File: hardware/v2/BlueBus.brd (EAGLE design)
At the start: 95 x 65 mm, 140 parts, among them J1 3PIN_953442_1, J2 6PIN_953442_1, J3 6PIN_5_103166_1, J4 SJ2-35853A-SMT-TR, J5 SMB_CONN, J6 USB3080-30-01-A, J7 PCM12SMTR, J8 TC2030NL, Q1 NMOSFET-BSS138K, Q2 NMOSFET-BSS138K, Q3 PMOSFET-DMP32D4SSOT323, U1 MPQ4420, U10 PCM5122, U11 PAM8406, U2 TH3122.4, U3 FT231XS, U4 S-1212BC0-U5T1U, U5 XC6210, U6 CAT25M01, U7 PIC24FJ1024GA606, U8 BM83SM1, U9 DIT4096

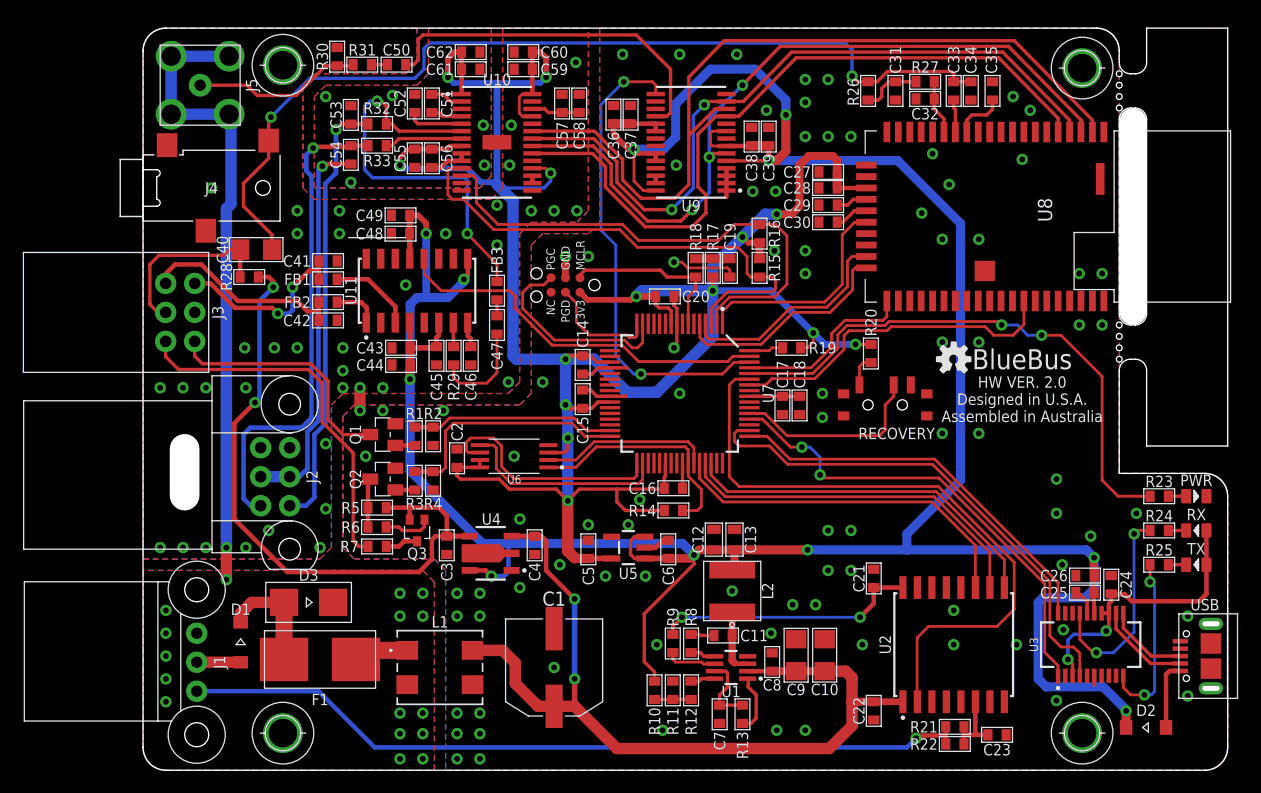
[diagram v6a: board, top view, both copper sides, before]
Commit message: [IMP] hardware: V2 silkscreen * Add fiducial markings * Fix issues with silkscreen
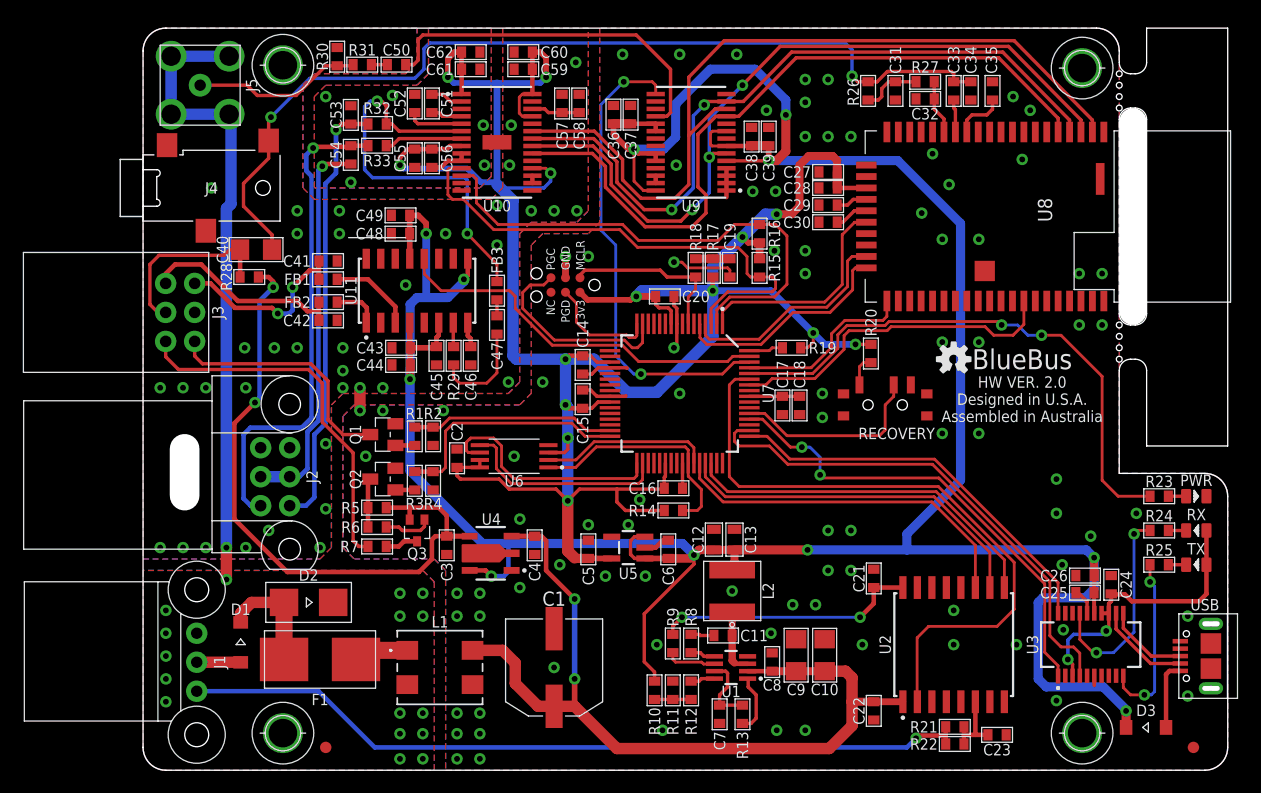
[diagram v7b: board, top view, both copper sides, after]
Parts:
- added FID1, FID2: FIDUCIAL_1MM, MF_Aesthetics:FIDUCIAL_1MM
- D2: value 2A_150V -> SMBJ18A; device Passives:SOD123FL-2 -> Passives:DO-214AA
- D3: value SMBJ18A -> 2A_150V; device Passives:DO-214AA -> Passives:SOD123FL-2
- moved D2 74.2 mm to (14.5, 14.7), turned to 180 degrees
- moved D3 74.2 mm to (87.8, 3.75), turned to 0 degrees
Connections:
- net 5V: now also D3.C; no longer D2.C
- net GND_FLT: now also D2.A; no longer D3.A
- net USB_5V: now also D3.A; no longer D2.A
- net VBAT_DIODE: now also D2.C; no longer D3.C
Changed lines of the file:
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@@
 <layer number="24" name="bOrigins" color="15" fill="1" visible="yes" active="yes"/>
 <layer number="25" name="tNames" color="7" fill="1" visible="yes" active="yes"/>
-<layer number="26" name="bNames" color="7" fill="1" visible="no" active="yes"/>
+<layer number="26" name="bNames" color="7" fill="1" visible="yes" active="yes"/>
 <layer number="27" name="tValues" color="7" fill="1" visible="no" active="yes"/>
 <layer number="28" name="bValues" color="7" fill="1" visible="no" active="yes"/>
@@
 <attribute name="PN" value="SMD2150PL-TP" x="8.55" y="11.2" size="1.778" layer="27" rot="R270" display="off"/>
 </element>
-<element name="D2" library="Passives" package="SOD123FL-2" value="2A_150V" x="87.85" y="3.75" smashed="yes">
+<element name="D3" library="Passives" package="SOD123FL-2" value="2A_150V" x="87.85" y="3.75" smashed="yes">
 <attribute name="MFG" value="MCC" x="141.19" y="-85.15" size="1.778" layer="27" display="off"/>
 <attribute name="NAME" x="87.85" y="4.75" size="1" layer="25" font="vector" ratio="15" align="bottom-center"/>
@@
 <element name="U3" library="ICs" package="SSOP20_L" value="FT231XS" x="83" y="11" smashed="yes">
 <attribute name="MFG" value="FTDI" x="83" y="11" size="1.778" layer="27" display="off"/>
-<attribute name="NAME" x="78.4" y="11" size="0.75" layer="25" font="vector" ratio="15" rot="R90" align="bottom-center"/>
+<attribute name="NAME" x="78.4" y="11" size="1" layer="25" font="vector" ratio="15" rot="R90" align="bottom-center"/>
 <attribute name="PN" value="FT231XS-R" x="83" y="11" size="1.778" layer="27" display="off"/>
 </element>
@@
 <element name="L2" library="Passives" package="MPL-SE5040" value="10uH" x="51.6" y="15.7" smashed="yes" rot="R270">
 <attribute name="MFG" value="Monolithic Power Systems" x="-10.63" y="-30.02" size="1.778" layer="27" rot="R270" display="off"/>
-<attribute name="NAME" x="54.2" y="15.7" size="1" layer="25" font="vector" ratio="15" rot="R90" align="top-center"/>
+<attribute name="NAME" x="54.25" y="15.7" size="1" layer="25" font="vector" ratio="15" rot="R90" align="top-center"/>
 <attribute name="PN" value="MPL-SE5040-100" x="-10.63" y="-30.02" size="1.778" layer="27" rot="R270" display="off"/>
 </element>
@@
 <element name="U10" library="ICs" package="TSSOP28" value="PCM5122" x="31" y="55" smashed="yes">
 <attribute name="MFG" value="Texas Instruments" x="31" y="55" size="1.778" layer="27" display="off"/>
-<attribute name="NAME" x="31" y="60" size="1" layer="25" font="vector" ratio="15" align="bottom-center"/>
+<attribute name="NAME" x="31" y="49.95" size="1" layer="25" font="vector" ratio="15" align="top-center"/>
 <attribute name="PN" value="PCM5122PW" x="31" y="55" size="1.778" layer="27" display="off"/>
 <attribute name="VALUE" value="PCM5122" x="31" y="55" size="1.778" layer="27" display="off"/>
@@
 <element name="U6" library="ICs" package="TSSOP-8" value="CAT25M01" x="32.5" y="27.5" smashed="yes" rot="R180">
 <attribute name="MFG" value="ONSEMI" x="32.5" y="27.5" size="1.778" layer="27" rot="R180" display="off"/>
-<attribute name="NAME" x="32.5" y="25.85" size="0.75" layer="21" font="vector" ratio="15" rot="R180" align="bottom-center"/>
+<attribute name="NAME" x="32.5" y="25.85" size="1" layer="21" font="vector" ratio="15" rot="R180" align="bottom-center"/>
 <attribute name="PN" value="CAT25M01YI-GT3" x="32.5" y="27.5" size="1.778" layer="27" rot="R180" display="off"/>
 </element>
@@
 <attribute name="PN" value="ERJ-PA3F1001V" x="23.8" y="25.35" size="1.778" layer="27" rot="R270" display="off"/>
 </element>
-<element name="D3" library="Passives" package="DO-214AA" value="SMBJ18A" x="14.5" y="14.7" smashed="yes" rot="R180">
+<element name="D2" library="Passives" package="DO-214AA" value="SMBJ18A" x="14.5" y="14.7" smashed="yes" rot="R180">
 <attribute name="MFG" value="Diodes" x="14.5" y="14.7" size="1.778" layer="27" rot="R180" display="off"/>
 <attribute name="NAME" x="14.5" y="16.6" size="1" layer="25" font="vector" ratio="15" rot="R180" align="top-center"/>
 <attribute name="PN" value="SMBJ18A-13-F" x="14.5" y="14.7" size="1.778" layer="27" rot="R180" display="off"/>
 </element>
+<element name="FID1" library="MF_Aesthetics" package="FIDUCIAL_1MM" value="FIDUCIAL_1MM" x="16" y="2" smashed="yes"/>
+<element name="FID2" library="MF_Aesthetics" package="FIDUCIAL_1MM" value="FIDUCIAL_1MM" x="92" y="2" smashed="yes"/>
 </elements>
 <signals>
@@
 <contactref element="U5" pad="3"/>
 <contactref element="U5" pad="1"/>
-<contactref element="D2" pad="C"/>
+<contactref element="D3" pad="C"/>
 <contactref element="C12" pad="1"/>
 <contactref element="C13" pad="1"/>
@@
 <signal name="USB_5V">
 <contactref element="J6" pad="1"/>
-<contactref element="D2" pad="A"/>
+<contactref element="D3" pad="A"/>
 <wire x1="90.85" y1="8.7" x2="89.9" y2="8.7" width="0.4" layer="1"/>
 <wire x1="89.9" y1="8.7" x2="89.6" y2="8.4" width="0.4" layer="1"/>
@@
 <contactref element="F1" pad="IN"/>
 <contactref element="D1" pad="C"/>
-<contactref element="D3" pad="C"/>
+<contactref element="D2" pad="C"/>
 <wire x1="8.55" y1="12.95" x2="8.55" y2="13.75" width="1" layer="1"/>
 <wire x1="8.55" y1="13.75" x2="8.9" y2="14.1" width="1" layer="1"/>
@@
 <wire x1="7.7" y1="57.3" x2="7.54" y2="57.46" width="1" layer="16"/>
 <wire x1="7.3" y1="19.5" x2="7.3" y2="49.2" width="1" layer="16"/>
-<contactref element="D3" pad="A"/>
+<contactref element="D2" pad="A"/>
 </signal>
 <signal name="MCU_VER">

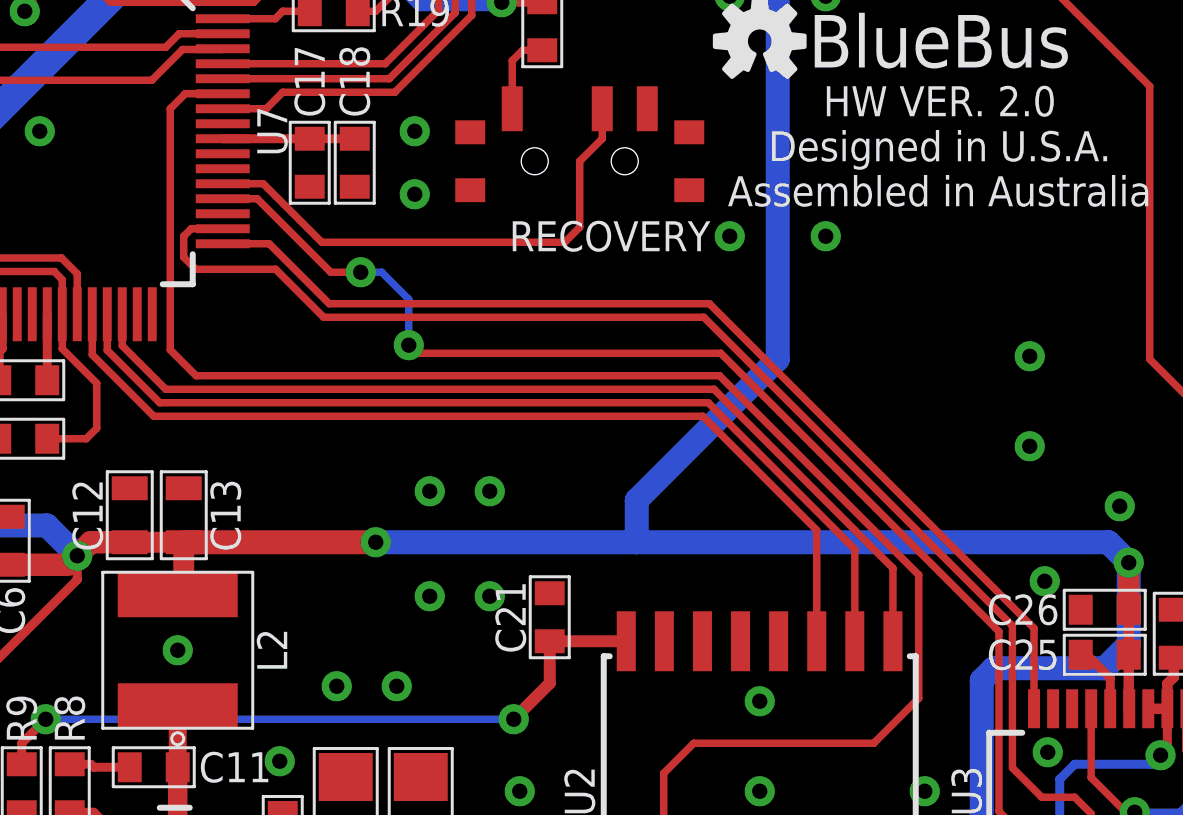
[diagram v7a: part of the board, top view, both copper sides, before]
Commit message: [IMP] hardware: V2 System UART Fix * Swap URX/UTX pins to maintain the same mapping as 1.x boards
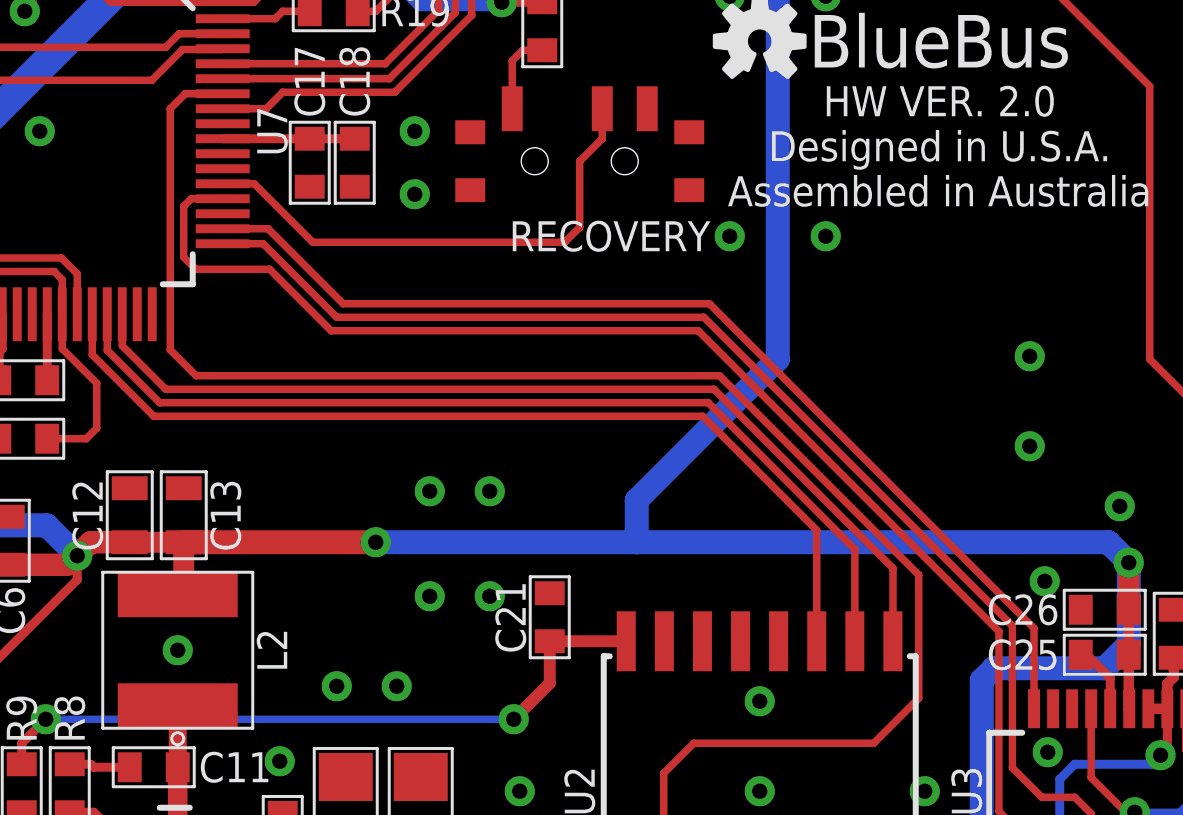
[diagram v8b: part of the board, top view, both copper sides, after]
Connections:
- net SYS_URX: now also U7.49; no longer U7.50
- net SYS_UTX: now also U7.50; no longer U7.49
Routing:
- net SYS_URX: track 44.8 -> 41.6 mm
- net SYS_DTR: track 41.3 -> 44.0 mm, vias 2 -> 0
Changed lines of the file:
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@@
 </signal>
 <signal name="SYS_URX" class="5">
-<contactref element="U7" pad="50"/>
 <contactref element="U3" pad="4"/>
-<wire x1="53.1" y1="29.75" x2="52.05" y2="29.75" width="0.25" layer="1"/>
-<wire x1="52.05" y1="29.75" x2="51.8" y2="29.5" width="0.25" layer="1"/>
-<wire x1="51.8" y1="29.5" x2="51.8" y2="28.8" width="0.25" layer="1"/>
-<wire x1="52.2" y1="28.4" x2="54.8636" y2="28.4" width="0.25" layer="1"/>
-<wire x1="51.8" y1="28.8" x2="52.2" y2="28.4" width="0.25" layer="1"/>
-<wire x1="56.4636" y1="26.8" x2="54.8636" y2="28.4" width="0.25" layer="1"/>
 <wire x1="80.4" y1="10.8" x2="81.5" y2="10.8" width="0.25" layer="1"/>
 <wire x1="81.5" y1="10.8" x2="82.0475" y2="10.2525" width="0.25" layer="1"/>
@@
 <wire x1="79.4228" y1="16.5136" x2="69.1364" y2="26.8" width="0.25" layer="1"/>
 <wire x1="79.4228" y1="11.7772" x2="79.4228" y2="16.5136" width="0.25" layer="1"/>
-<wire x1="69.1364" y1="26.8" x2="56.4636" y2="26.8" width="0.25" layer="1"/>
+<wire x1="69.1364" y1="26.8" x2="56.9" y2="26.8" width="0.25" layer="1"/>
+<contactref element="U7" pad="49"/>
+<wire x1="53.1" y1="29.25" x2="54.45" y2="29.25" width="0.25" layer="1"/>
+<wire x1="54.45" y1="29.25" x2="56.9" y2="26.8" width="0.25" layer="1"/>
 </signal>
 <signal name="SYS_UTX" class="5">
-<contactref element="U7" pad="49"/>
 <contactref element="U3" pad="20"/>
-<wire x1="53.1" y1="29.25" x2="54.65" y2="29.25" width="0.25" layer="1"/>
-<wire x1="54.65" y1="29.25" x2="56.65" y2="27.25" width="0.25" layer="1"/>
 <wire x1="80.1425" y1="16.4303" x2="80.1425" y2="13.75" width="0.25" layer="1"/>
-<wire x1="56.65" y1="27.25" x2="69.3228" y2="27.25" width="0.25" layer="1"/>
+<wire x1="57.1136" y1="27.25" x2="69.3228" y2="27.25" width="0.25" layer="1"/>
 <wire x1="69.3228" y1="27.25" x2="80.1425" y2="16.4303" width="0.25" layer="1"/>
+<contactref element="U7" pad="50"/>
+<wire x1="53.1" y1="29.75" x2="54.6136" y2="29.75" width="0.25" layer="1"/>
+<wire x1="57.1136" y1="27.25" x2="54.6136" y2="29.75" width="0.25" layer="1"/>
 </signal>
 <signal name="IBUS_UTX" class="5">
@@
 <contactref element="U3" pad="1"/>
 <wire x1="80.1425" y1="9.1575" x2="80.1425" y2="8.25" width="0.25" layer="1"/>
-<wire x1="53.1" y1="30.75" x2="54.25" y2="30.75" width="0.25" layer="1"/>
-<wire x1="56.7" y1="28.3" x2="57.7" y2="28.3" width="0.25" layer="1"/>
-<via x="57.7" y="28.3" extent="1-16" drill="0.51"/>
-<wire x1="54.25" y1="30.75" x2="56.7" y2="28.3" width="0.25" layer="1"/>
-<wire x1="57.7" y1="28.3" x2="58.4" y2="28.3" width="0.25" layer="16"/>
-<wire x1="59.3" y1="27.4" x2="59.3" y2="25.87" width="0.25" layer="16"/>
-<via x="59.3" y="25.87" extent="1-16" drill="0.51"/>
-<wire x1="59.3" y1="25.87" x2="59.57" y2="25.6" width="0.25" layer="1"/>
-<wire x1="58.4" y1="28.3" x2="59.3" y2="27.4" width="0.25" layer="16"/>
 <wire x1="78.9728" y1="16.3272" x2="78.9728" y2="10.3272" width="0.25" layer="1"/>
-<wire x1="59.57" y1="25.6" x2="69.7" y2="25.6" width="0.25" layer="1"/>
-<wire x1="69.7" y1="25.6" x2="78.9728" y2="16.3272" width="0.25" layer="1"/>
+<wire x1="68.95" y1="26.35" x2="78.9728" y2="16.3272" width="0.25" layer="1"/>
 <wire x1="78.9728" y1="10.3272" x2="80.1425" y2="9.1575" width="0.25" layer="1"/>
+<wire x1="53.1" y1="30.75" x2="52.05" y2="30.75" width="0.25" layer="1"/>
+<wire x1="52.05" y1="30.75" x2="51.8" y2="30.5" width="0.25" layer="1"/>
+<wire x1="51.8" y1="30.5" x2="51.8" y2="28.8" width="0.25" layer="1"/>
+<wire x1="52.2" y1="28.4" x2="54.6636" y2="28.4" width="0.25" layer="1"/>
+<wire x1="56.7136" y1="26.35" x2="68.95" y2="26.35" width="0.25" layer="1"/>
+<wire x1="51.8" y1="28.8" x2="52.2" y2="28.4" width="0.25" layer="1"/>
+<wire x1="54.6636" y1="28.4" x2="56.7136" y2="26.35" width="0.25" layer="1"/>
 </signal>
 <signal name="IBUS_FILT">
@@
 <contactref element="J7" pad="2"/>
 <contactref element="U7" pad="53"/>
-<wire x1="53.1" y1="31.25" x2="54.45" y2="31.25" width="0.25" layer="1"/>
-<wire x1="54.45" y1="31.25" x2="56.4" y2="29.3" width="0.25" layer="1"/>
-<wire x1="64.5" y1="29.3" x2="56.4" y2="29.3" width="0.25" layer="1"/>
+<wire x1="53.1" y1="31.25" x2="54.15" y2="31.25" width="0.25" layer="1"/>
+<wire x1="54.15" y1="31.25" x2="56.1" y2="29.3" width="0.25" layer="1"/>
+<wire x1="64.5" y1="29.3" x2="56.1" y2="29.3" width="0.25" layer="1"/>
 <wire x1="65.75" y1="33.75" x2="65.75" y2="32.75" width="0.25" layer="1"/>
 <wire x1="65" y1="29.8" x2="64.5" y2="29.3" width="0.25" layer="1"/>
